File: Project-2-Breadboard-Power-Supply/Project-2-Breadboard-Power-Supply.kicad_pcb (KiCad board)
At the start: 2 copper layers, 35.1 x 53.3 mm, 16 parts, among them J1 Conn_01x02_Pin, J2 Conn_01x02_Pin, J3 Conn_01x03_Pin, J4 Conn_01x03_Pin, J5 Screw_Terminal_01x02, J6 Barrel_Jack_Switch, J7 Screw_Terminal_01x02, U1 LM7805_TO220, U2 LM317_TO-220

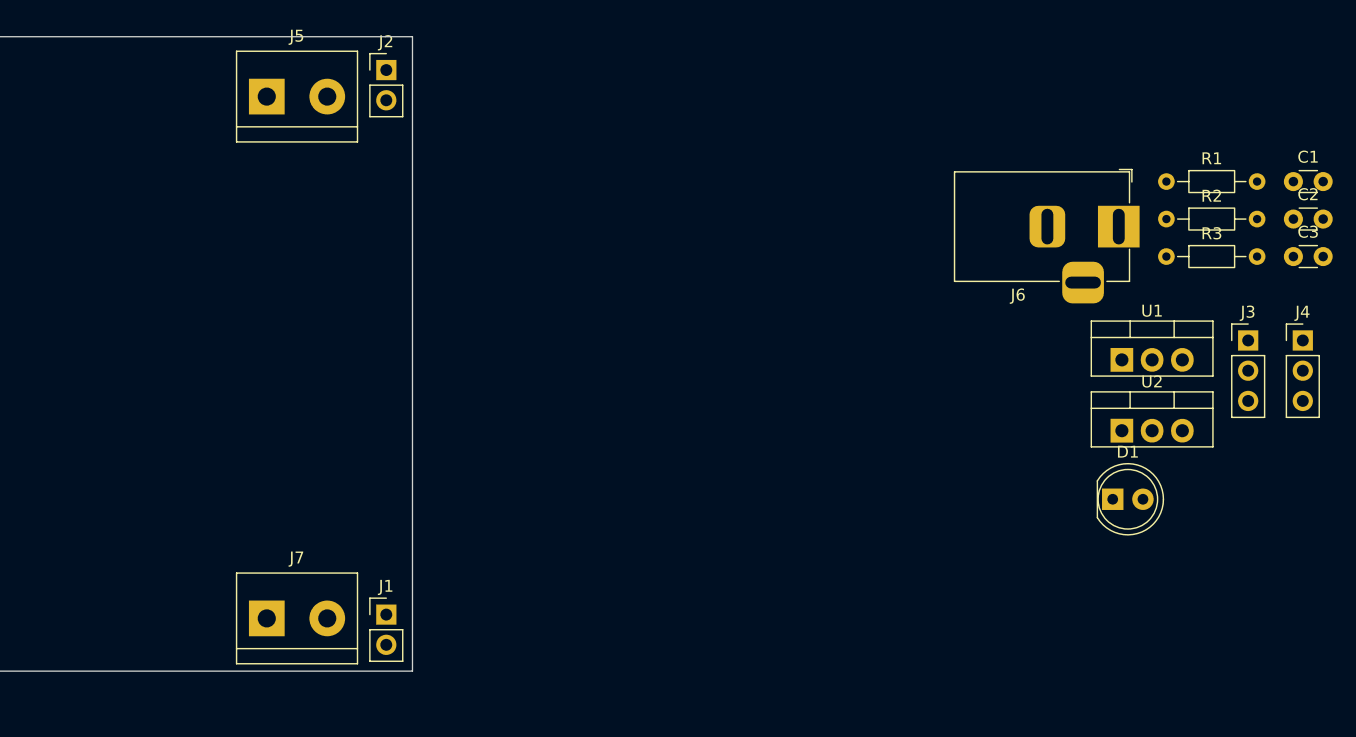
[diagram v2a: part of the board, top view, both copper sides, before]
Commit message: bugfix: add and assign missing library symbol and footprint
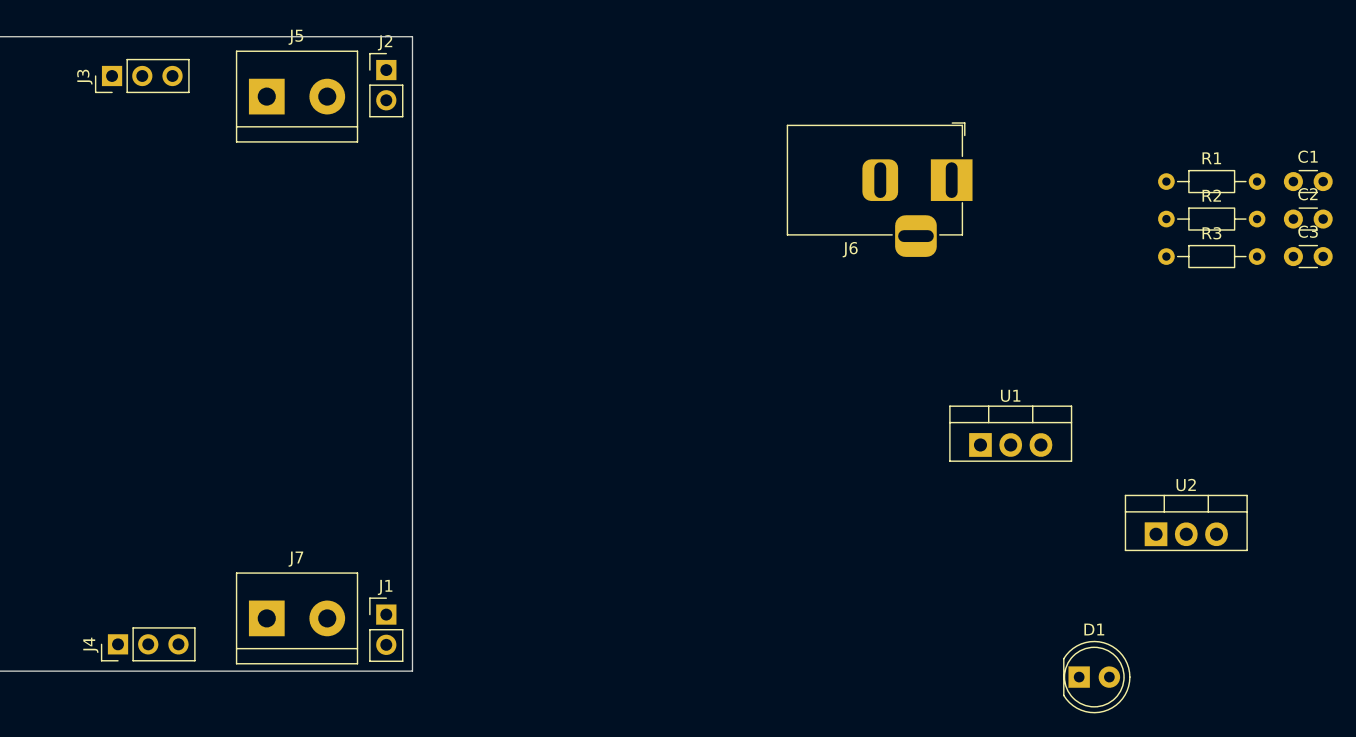
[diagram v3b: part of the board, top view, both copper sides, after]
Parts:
- moved J4 102.8 mm to (38.5, 95.8), turned to 90 degrees
- moved J3 98.0 mm to (38.0, 48.0), turned to 90 degrees
- moved D1 15.2 mm to (119.2, 98.5)
- moved J6 14.6 mm to (108.5, 56.8)
- moved U1 13.9 mm to (110.9, 79.0)
- moved U2 9.16 mm to (125.7, 86.5)
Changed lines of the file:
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@@
 	(footprint "Connector_PinHeader_2.54mm:PinHeader_1x03_P2.54mm_Vertical"
 		(layer "F.Cu")
-		(at 138 70.22)
+		(at 38.46 95.75 90)
 		(descr "Through hole straight pin header, 1x03, 2.54mm pitch, single row")
 		(tags "Through hole pin header THT 1x03 2.54mm single row")
 		(property "Reference" "J4"
-			(at 0 -2.38 0)
+			(at 0 -2.38 90)
 			(layer "F.SilkS")
 			(effects
@@
 		)
 		(property "Value" "Conn_01x03_Pin"
-			(at 0 7.46 0)
+			(at 0 7.46 90)
 			(layer "F.Fab")
 			(effects
@@
 		)
 		(property "Datasheet" ""
-			(at 0 0 0)
+			(at 0 0 90)
 			(layer "F.Fab")
 			(hide yes)
@@
 		)
 		(property "Description" "Generic connector, single row, 01x03, script generated"
-			(at 0 0 0)
+			(at 0 0 90)
 			(layer "F.Fab")
 			(hide yes)
@@
 		)
 		(property "KiLib_Generator" "connector/pin_header_socket"
-			(at 0 0 0)
+			(at 0 0 90)
 			(layer "F.SilkS")
 			(hide yes)
@@
 		)
 		(property "MPN" ""
-			(at 0 0 0)
+			(at 0 0 90)
 			(unlocked yes)
 			(layer "F.Fab")
@@
 		)
 		(property "Manufacturer" ""
-			(at 0 0 0)
+			(at 0 0 90)
 			(unlocked yes)
 			(layer "F.Fab")
@@
 		)
 		(property "Purpose" "Output voltage selector #2"
-			(at 0 0 0)
+			(at 0 0 90)
 			(unlocked yes)
 			(layer "F.Fab")
@@
 		)
 		(fp_line
-			(start -1.38 1.27)
-			(end -1.38 6.46)
+			(start 1.38 1.27)
+			(end 1.38 6.46)
 			(stroke
 				(width 0.12)
@@
 		)
 		(fp_line
-			(start -1.38 6.46)
-			(end 1.38 6.46)
+			(start -1.38 1.27)
+			(end -1.38 6.46)
 			(stroke
 				(width 0.12)
@@
 		)
 		(fp_line
-			(start 1.38 1.27)
+			(start -1.38 6.46)
 			(end 1.38 6.46)
 			(stroke
@@
 		)
 		(fp_line
-			(start -1.27 -0.635)
-			(end -0.635 -1.27)
+			(start 1.27 -1.27)
+			(end 1.27 6.35)
 			(stroke
 				(width 0.1)
@@
 		)
 		(fp_line
-			(start -1.27 6.35)
-			(end -1.27 -0.635)
+			(start -0.635 -1.27)
+			(end 1.27 -1.27)
 			(stroke
 				(width 0.1)
@@
 		)
 		(fp_line
-			(start -0.635 -1.27)
-			(end 1.27 -1.27)
+			(start -1.27 -0.635)
+			(end -0.635 -1.27)
 			(stroke
 				(width 0.1)
@@
 		)
 		(fp_line
-			(start 1.27 -1.27)
-			(end 1.27 6.35)
+			(start 1.27 6.35)
+			(end -1.27 6.35)
 			(stroke
 				(width 0.1)
@@
 		)
 		(fp_line
-			(start 1.27 6.35)
-			(end -1.27 6.35)
+			(start -1.27 6.35)
+			(end -1.27 -0.635)
 			(stroke
 				(width 0.1)
@@
 		)
 		(fp_text user "${REFERENCE}"
-			(at 0 2.54 90)
+			(at 0 2.54 0)
 			(layer "F.Fab")
 			(effects
@@
 		)
 		(pad "1" thru_hole rect
-			(at 0 0)
+			(at 0 0 90)
 			(size 1.7 1.7)
 			(drill 1)
@@
 		)
 		(pad "2" thru_hole circle
-			(at 0 2.54)
+			(at 0 2.54 90)
 			(size 1.7 1.7)
 			(drill 1)
@@
 		)
 		(pad "3" thru_hole circle
-			(at 0 5.08)
+			(at 0 5.08 90)
 			(size 1.7 1.7)
 			(drill 1)
@@
 	(footprint "LED_THT:LED_D5.0mm"
 		(layer "F.Cu")
-		(at 122.03 83.56)
+		(at 119.21 98.5)
 		(descr "LED, diameter 5.0mm, 2 pins, http://cdn-reichelt.de/documents/datenblatt/A500/LL-504BC2E-009.pdf, generated by kicad-footprint-generator")
 		(tags "LED")
@@
 		)
 		(point
-			(at 123.3 83.56)
+			(at 120.48 98.5)
 			(size 2)
 			(layer "F.Fab")
@@
 	(footprint "Connector_PinHeader_2.54mm:PinHeader_1x03_P2.54mm_Vertical"
 		(layer "F.Cu")
-		(at 133.41 70.22)
+		(at 37.96 48 90)
 		(descr "Through hole straight pin header, 1x03, 2.54mm pitch, single row")
 		(tags "Through hole pin header THT 1x03 2.54mm single row")
 		(property "Reference" "J3"
-			(at 0 -2.38 0)
+			(at 0 -2.38 90)
 			(layer "F.SilkS")
 			(effects
@@
 		)
 		(property "Value" "Conn_01x03_Pin"
-			(at 0 7.46 0)
+			(at 0 7.46 90)
 			(layer "F.Fab")
 			(effects
@@
 		)
 		(property "Datasheet" ""
-			(at 0 0 0)
+			(at 0 0 90)
 			(layer "F.Fab")
 			(hide yes)
@@
 		)
 		(property "Description" "Generic connector, single row, 01x03, script generated"
-			(at 0 0 0)
+			(at 0 0 90)
 			(layer "F.Fab")
 			(hide yes)
@@
 		)
 		(property "KiLib_Generator" "connector/pin_header_socket"
-			(at 0 0 0)
+			(at 0 0 90)
 			(layer "F.SilkS")
 			(hide yes)
@@
 		)
 		(property "MPN" ""
-			(at 0 0 0)
+			(at 0 0 90)
 			(unlocked yes)
 			(layer "F.Fab")
@@
 		)
 		(property "Manufacturer" ""
-			(at 0 0 0)
+			(at 0 0 90)
 			(unlocked yes)
 			(layer "F.Fab")
@@
 		)
 		(property "Purpose" "Output voltage selector #1"
-			(at 0 0 0)
+			(at 0 0 90)
 			(unlocked yes)
 			(layer "F.Fab")
@@
 		)
 		(fp_line
-			(start -1.38 1.27)
-			(end -1.38 6.46)
+			(start 1.38 1.27)
+			(end 1.38 6.46)
 			(stroke
 				(width 0.12)
@@
 		)
 		(fp_line
-			(start -1.38 6.46)
-			(end 1.38 6.46)
+			(start -1.38 1.27)
+			(end -1.38 6.46)
 			(stroke
 				(width 0.12)
@@
 		)
 		(fp_line
-			(start 1.38 1.27)
+			(start -1.38 6.46)
 			(end 1.38 6.46)
 			(stroke
@@
 		)
 		(fp_line
-			(start -1.27 -0.635)
-			(end -0.635 -1.27)
+			(start 1.27 -1.27)
+			(end 1.27 6.35)
 			(stroke
 				(width 0.1)
@@
 		)
 		(fp_line
-			(start -1.27 6.35)
-			(end -1.27 -0.635)
+			(start -0.635 -1.27)
+			(end 1.27 -1.27)
 			(stroke
 				(width 0.1)
@@
 		)
 		(fp_line
-			(start -0.635 -1.27)
-			(end 1.27 -1.27)
+			(start -1.27 -0.635)
+			(end -0.635 -1.27)
 			(stroke
 				(width 0.1)
@@
 		)
 		(fp_line
-			(start 1.27 -1.27)
-			(end 1.27 6.35)
+			(start 1.27 6.35)
+			(end -1.27 6.35)
 			(stroke
 				(width 0.1)
@@
 		)
 		(fp_line
-			(start 1.27 6.35)
-			(end -1.27 6.35)
+			(start -1.27 6.35)
+			(end -1.27 -0.635)
 			(stroke
 				(width 0.1)
@@
 		)
 		(fp_text user "${REFERENCE}"
-			(at 0 2.54 90)
+			(at 0 2.54 0)
 			(layer "F.Fab")
 			(effects
@@
 		)
 		(pad "1" thru_hole rect
-			(at 0 0)
+			(at 0 0 90)
 			(size 1.7 1.7)
 			(drill 1)
@@
 		)
 		(pad "2" thru_hole circle
-			(at 0 2.54)
+			(at 0 2.54 90)
 			(size 1.7 1.7)
 			(drill 1)
@@
 		)
 		(pad "3" thru_hole circle
-			(at 0 5.08)
+			(at 0 5.08 90)
 			(size 1.7 1.7)
 			(drill 1)
@@
 	(footprint "Package_TO_SOT_THT:TO-220-3_Vertical"
 		(layer "F.Cu")
-		(at 122.8 77.8)
+		(at 125.67 86.5)
 		(descr "TO-220-3, Vertical, RM 2.54mm, see https://www.vishay.com/docs/66542/to-220-1.pdf")
 		(tags "TO-220-3 Vertical RM 2.54mm")
@@
 	(footprint "Connector_BarrelJack:BarrelJack_Horizontal"
 		(layer "F.Cu")
-		(at 122.54 60.655)
+		(at 108.5 56.75)
 		(descr "DC Barrel Jack")
 		(tags "Power Jack")
@@
 	(footprint "Package_TO_SOT_THT:TO-220-3_Vertical"
 		(layer "F.Cu")
-		(at 122.8 71.85)
+		(at 110.92 79)
 		(descr "TO-220-3, Vertical, RM 2.54mm, see https://www.vishay.com/docs/66542/to-220-1.pdf")
 		(tags "TO-220-3 Vertical RM 2.54mm")

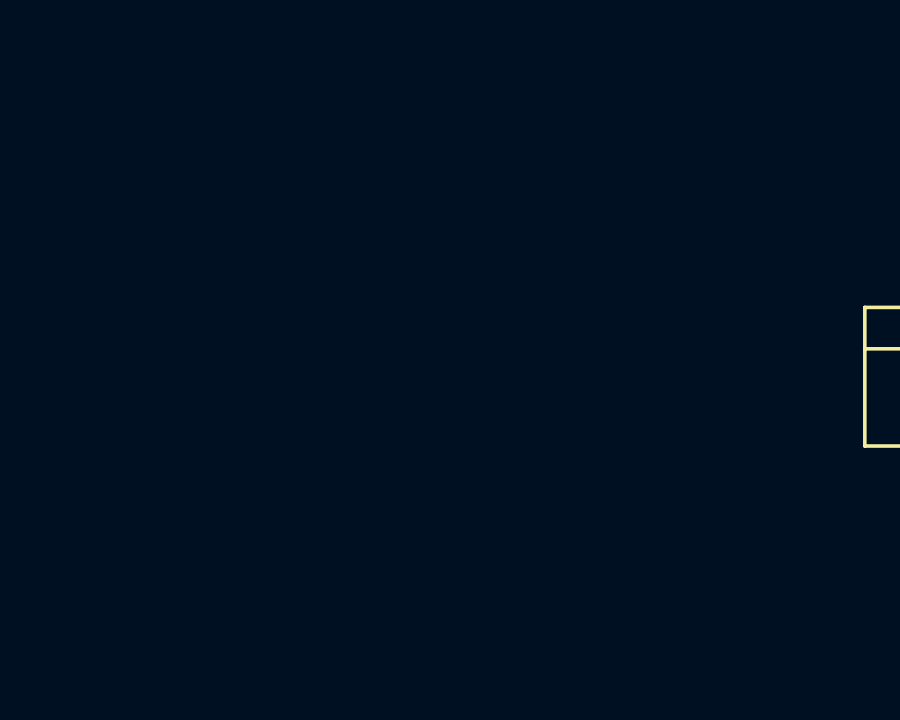
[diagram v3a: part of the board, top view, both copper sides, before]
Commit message: update pcb with missing switch footprint, from schematic metadata
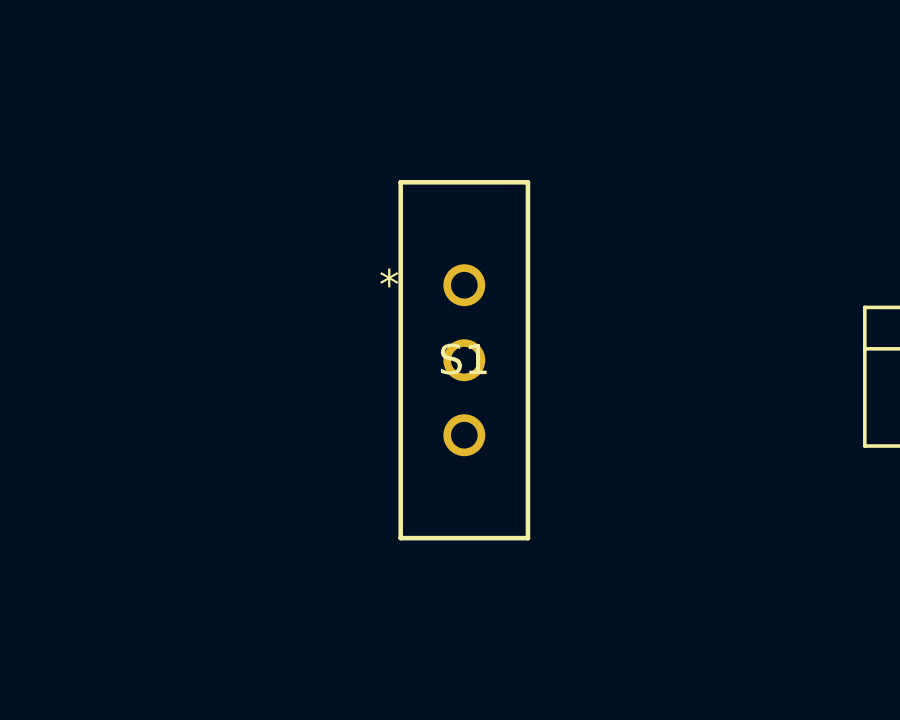
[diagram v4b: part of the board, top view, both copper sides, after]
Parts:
- added S1: EG1218, Custom_Library_0.pretty:SW_1218_EWI, F.Cu at (95.0, 75.0)

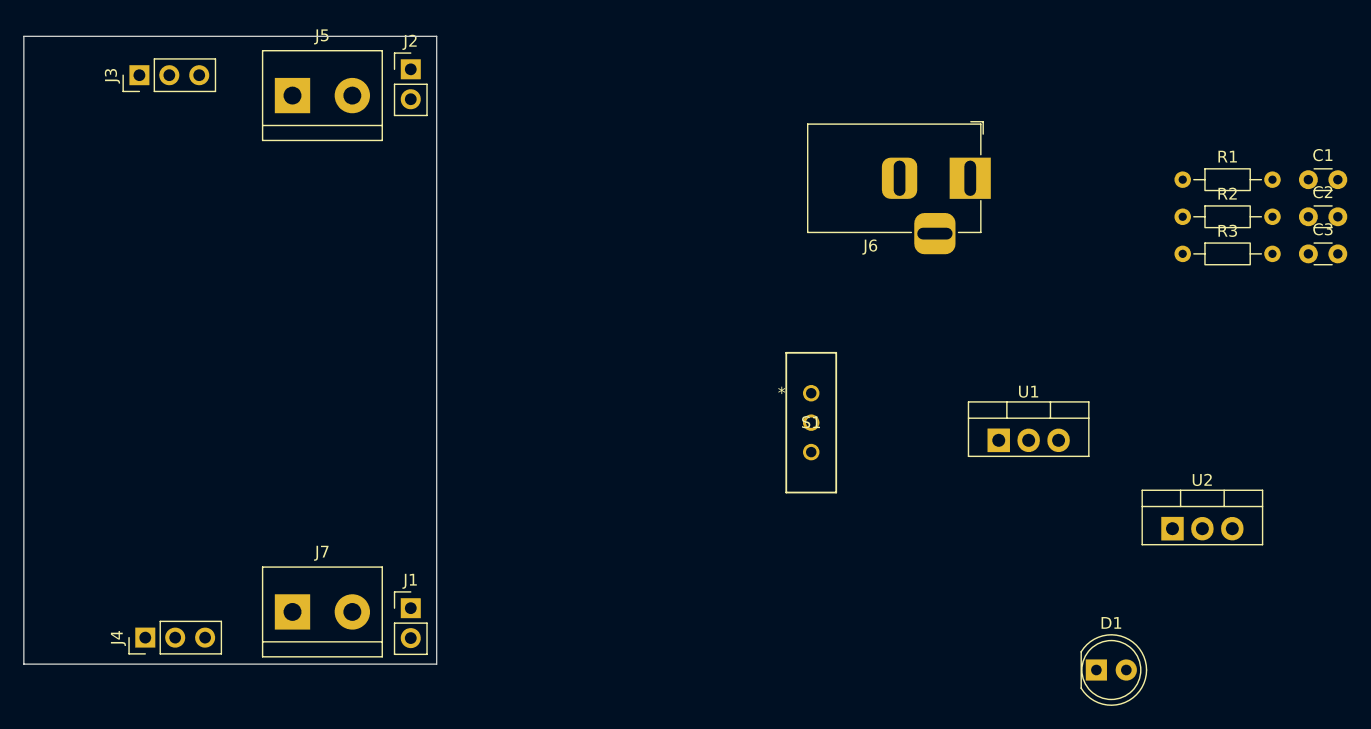
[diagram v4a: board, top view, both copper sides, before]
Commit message: place components' footprints on PCB, and lock them in place
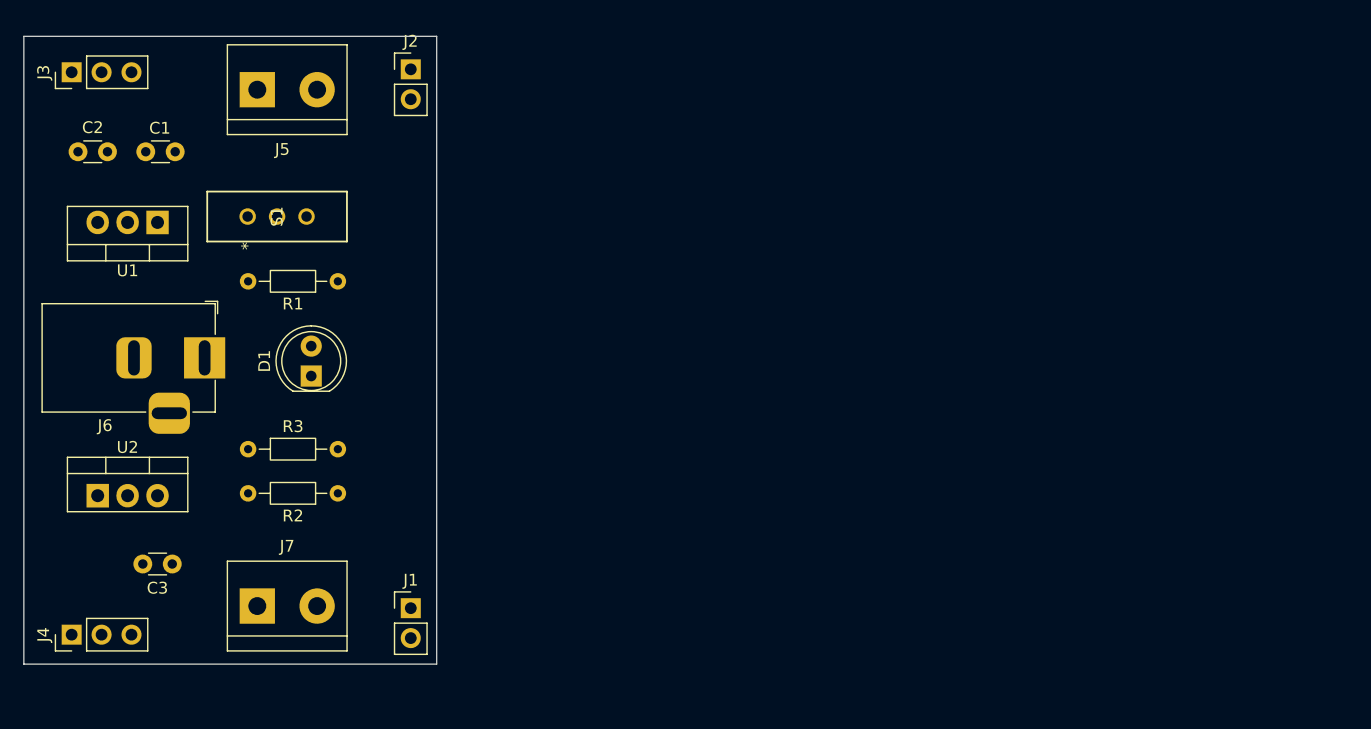
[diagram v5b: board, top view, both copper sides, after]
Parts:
- moved C2 104.6 mm to (32.8, 54.5)
- moved C3 100.0 mm to (40.8, 89.5), turned to 180 degrees
- moved C1 96.2 mm to (41.0, 54.5), turned to 180 degrees
- moved U2 91.3 mm to (34.4, 83.7)
- moved R3 81.1 mm to (47.2, 79.8)
- moved R2 75.5 mm to (54.8, 83.5), turned to 180 degrees
- moved U1 73.8 mm to (39.5, 60.5), turned to 180 degrees
- moved R1 72.2 mm to (54.8, 65.5), turned to 180 degrees
- moved D1 71.2 mm to (52.5, 73.5), turned to 90 degrees
- moved J6 66.8 mm to (43.5, 72.0)
- moved S1 50.1 mm to (47.2, 60.0), turned to 90 degrees
- moved J4 6.25 mm to (32.2, 95.5)
- moved J3 5.76 mm to (32.2, 47.8)
- moved J5 3.03 mm to (48.0, 49.2)
- moved J7 3.03 mm to (48.0, 93.1)
